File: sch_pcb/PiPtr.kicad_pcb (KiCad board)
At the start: 4 copper layers, 101.6 x 141.7 mm, 384 parts, among them J101 GLOBAL_LINK_LEFT, J102 GLOBAL_LINK_RIGHT, J107 RASPBERRY_PI, J111 FP_PIXEL, J112 AM2302, J204 DE9F, J305 AUX_IO_1, J306 SPARE, J307 SPARE, J308 AUX_IO_2, J311 I2C1_5V, J312 RTC, J315 OLED_SSD1306, J404 DE9F, J501 MicroUSB, P301 Chassis, Q101 BSS138, Q102 BSS138, Q103 BSS138, Q104 BSS138, Q105 BSS138, Q201 BSS138, Q202 BSS138, Q203 BSS138, Q401 BSS138, Q402 BSS138, Q403 BSS138, Q501 BSR315PH6327XTSA1, U101 MCP23008, U102 IP4234CZ6, U103 MCP4351, U104 74HCT138, U105 74LV1T125, U106 MCP6004T, U107 MCP4351, U108 74LVC4066, U109 74LVC1G3157, U110 74LV1T125, U111 74LV1T125, U112 74LV1T125, U113 74LV1T125, U201 MCP6004T, U202 74LVC1G3157, U203 74LVC1G3157, U204 74LVC4066, U205 MCP6004T, U206 74LVC1G3157, U207 MCP6S26, U208 MCP23008, U301 MCP23017, U304 MCP3008, U305 MCP1703A-2502/MB, U306 TPS54302, U307 IP4234CZ6, U308 IP4234CZ6, U401 MCP6004T, U402 74LVC1G3157, U403 74LVC1G3157, U404 74LVC4066, U405 MCP6004T, U406 74LVC1G3157, U407 MCP6S26, U408 MCP23008, U501 CM108B, U502 CM108B, U503 TUSB2036, U504 MCP1703A-3302/MB, U505 CM108B, Y501 6MHz

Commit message: BOM scrub
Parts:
- C501, C503, C505, C507, C513, C514, C515, C516, C517, C518, C519, C520, C533, C534, C535, C537, C538, C539: value 4u7 -> 4.7u
- C502, C504, C506, C508, C521, C522, C536, C543: value 100n -> 0.1u
- C509, C510, C511, C512, C527, C528, C540, C541, C542: footprint lib:smd0603 -> lib:smd0805
- R120: value 2200 -> 2k2
- R122: value 3300 -> 3k3
- R124: value 330R -> 100
- R214, R414: value 13k7 -> 13k3
- R325: value 511k -> SPARE
- R326: value 105k -> SPARE
- R327: value 150k -> 100k
- R503, R504, R505, R506, R507, R508, R519, R520: value 22R -> 22
- R515, R516, R523: value 33R -> 33
- moved C538 1.16 mm to (113.3, 109.0)
- moved C542 0.94 mm to (112.9, 110.4)
- moved C514 0.84 mm to (141.2, 119.5)
- moved C513 0.72 mm to (122.8, 119.7)
- moved C512 0.69 mm to (141.2, 121.1)
- moved C511 0.60 mm to (122.8, 121.2)
- moved C540 0.56 mm to (112.9, 112.1)
- moved C528 0.31 mm to (141.2, 122.9)
- moved C527 0.28 mm to (122.8, 122.9)
- moved C541 0.24 mm to (112.9, 113.9)
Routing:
- net Net-(C514-Pad1): track 3.35 -> 6.25 mm
- net Net-(C538-Pad1): track 3.11 -> 5.80 mm
- net /soundcard/TO_SND3: track 17.2 -> 16.1 mm
- net Net-(C513-Pad1): track 3.19 -> 4.14 mm
- net /soundcard/FROM_SND3: track 18.6 -> 17.8 mm
- net /soundcard/TO_SND2: track 46.6 -> 45.8 mm
- net /soundcard/FROM_SND2: track 56.8 -> 56.1 mm

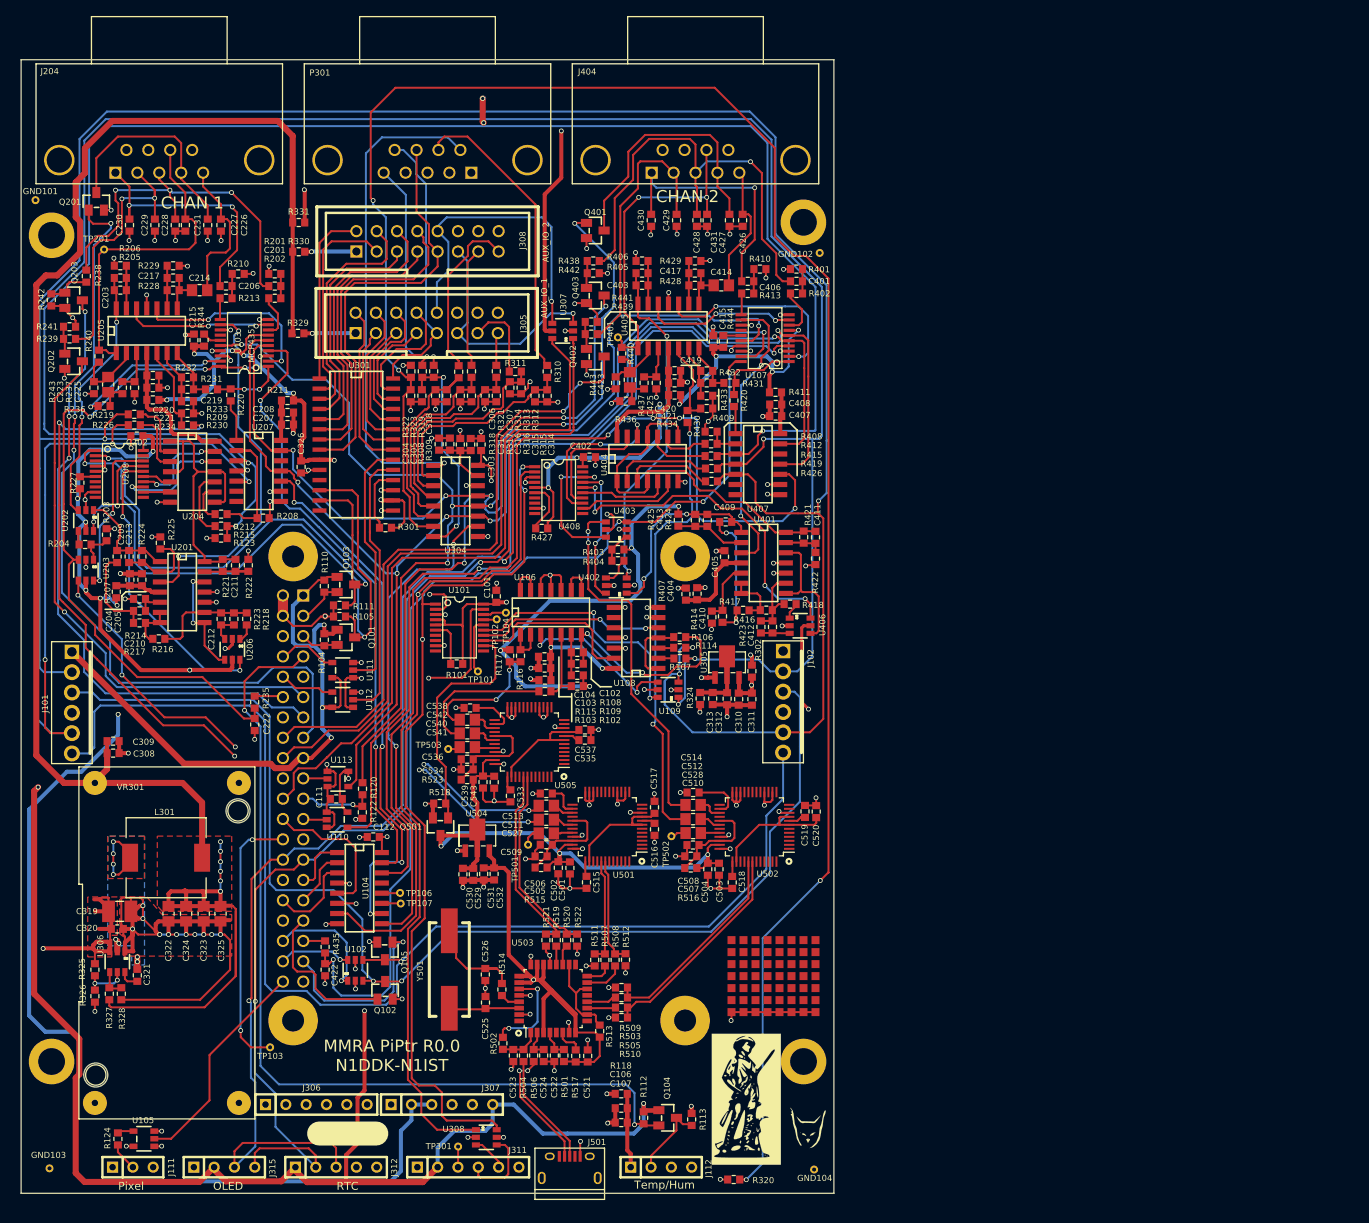
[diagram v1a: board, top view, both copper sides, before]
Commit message: Move link connector close to edge to allow using jumpers to connect boards
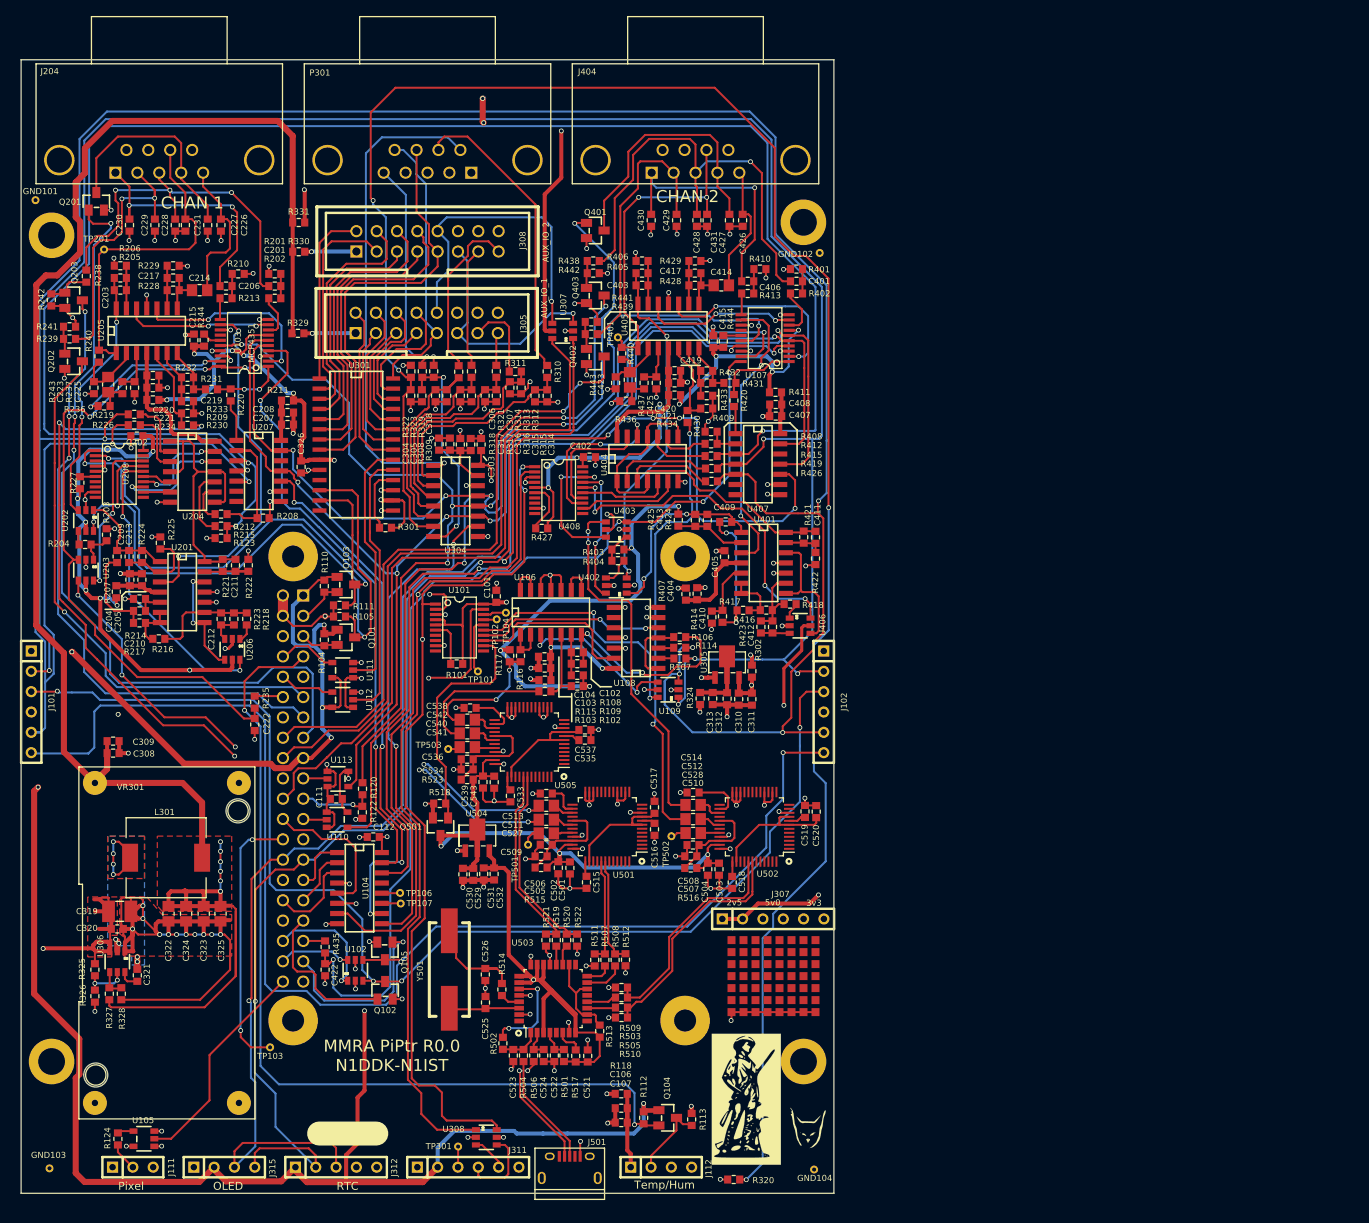
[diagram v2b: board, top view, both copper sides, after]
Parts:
- removed J306: SPARE, lib:SIL-6
- J101, J102: footprint lib:Molex_22-27-2061_100mil_6pin_verical -> lib:SIL-6
- moved J307 47.5 mm to (151.2, 135.3)
- moved J101 5.08 mm to (58.4, 108.2)
- moved J102 5.08 mm to (157.5, 108.2)
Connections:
- J307 pad 1: (no net) -> +2V5
- J307 pad 3: +2V5 -> +5V
- J307 pad 5: +5V -> +3V3
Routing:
- net +2V5: track 232.8 -> 151.7 mm, vias 38 -> 39
- net +3V3: track 528.5 -> 561.9 mm, vias 10 -> 11
- net /LINK2C: track 156.1 -> 164.8 mm, vias 1 -> 2
- net LINK2_AUD: track 370.8 -> 365.3 mm
- net /LINK1C: track 151.2 -> 155.8 mm, vias 2 -> 4
- net +5V: track 534.7 -> 532.5 mm
- net /soundcard/U2N: track 27.2 -> 29.2 mm
- net /soundcard/U2P: track 26.1 -> 28.0 mm
- net LINK1_AUD: track 302.2 -> 303.9 mm, vias 5 -> 7
- net /Spares, GPIO, and ADC/ADC_LIGHT: track 250.5 -> 251.8 mm
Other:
- board text added: "2v5"
- board text added: "3v3"
- board text added: "5v0"

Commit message: Change 33pf to 100pf.  Change 2k and 2200 to 2k2.  Change I2C addresses for MCP23008.  Nudge link connectors
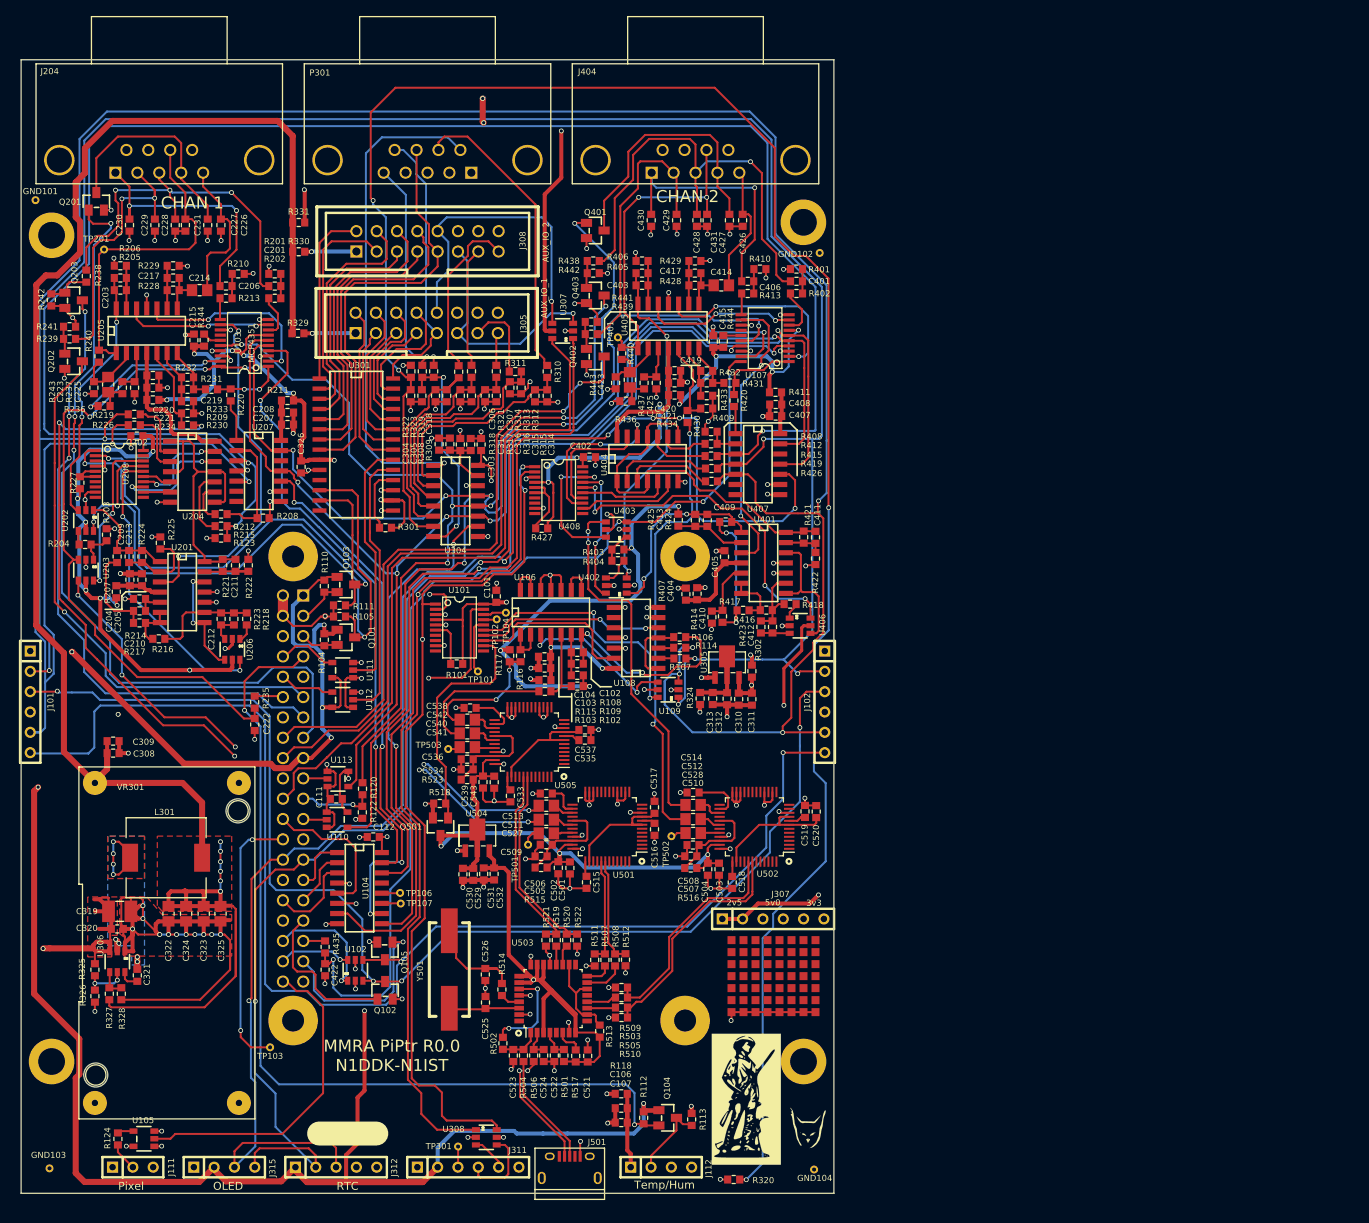
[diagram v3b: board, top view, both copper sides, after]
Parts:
- C102, C203, C211, C213, C217, C219, C403, C411, C413, C417, C419: value 33p -> 100p
- R104, R105, R107, R110, R111, R114, R212, R215, R219, R226, R412, R415, R419, R426: value 2k -> 2k2
- R308: value 2200 -> 2k2
- moved J102 0.13 mm to (157.6, 108.2)
- moved J101 0.13 mm to (58.3, 108.2)
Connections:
- J112 pad 3: (no net) -> Net-(J112-Pad3)
- J305 pad 16: (no net) -> Net-(J305-Pad16)
- J308 pad 16: (no net) -> Net-(J308-Pad16)
- J312 pad 4: Net-(J312-Pad4) -> (no net)
- J501 pad 1: (no net) -> Net-(J501-Pad1)
- J501 pad 4: (no net) -> Net-(J501-Pad4)
- MTG301 pad 1: (no net) -> Net-(MTG301-Pad1)
- MTG302 pad 1: (no net) -> Net-(MTG302-Pad1)
- MTG303 pad 1: (no net) -> Net-(MTG303-Pad1)
- MTG304 pad 1: (no net) -> Net-(MTG304-Pad1)
- U101 pad 10: Net-(U101-Pad10) -> (no net)
- U101 pad 11: Net-(U101-Pad11) -> (no net)
- U101 pad 5: +5V -> GND
- U101 pad 7: Net-(U101-Pad7) -> (no net)
- U101 pad 8: Net-(U101-Pad8) -> (no net)
- U104 pad 13: (no net) -> Net-(U104-Pad13)
- U108 pad 10: Net-(U108-Pad10) -> (no net)
- U108 pad 9: Net-(U108-Pad9) -> (no net)
- U207 pad 12: (no net) -> Net-(U207-Pad12)
- U207 pad 6: (no net) -> Net-(U207-Pad6)
- U207 pad 7: (no net) -> Net-(U207-Pad7)
- U208 pad 10: Net-(U208-Pad10) -> (no net)
- U208 pad 11: Net-(U208-Pad11) -> (no net)
- U208 pad 19: Net-(U208-Pad19) -> (no net)
- U208 pad 5: GND -> Net-(R227-Pad1)
- U208 pad 7: Net-(U208-Pad7) -> (no net)
- U208 pad 8: Net-(U208-Pad8) -> (no net)
- U407 pad 12: (no net) -> Net-(U407-Pad12)
- U407 pad 6: (no net) -> Net-(U407-Pad6)
- U407 pad 7: (no net) -> Net-(U407-Pad7)
- U408 pad 10: (no net) -> Net-(U408-Pad10)
- U408 pad 11: (no net) -> Net-(U408-Pad11)
- U408 pad 19: (no net) -> Net-(U408-Pad19)
- U408 pad 4: GND -> +5V
- U408 pad 5: +5V -> Net-(R427-Pad1)
- U408 pad 7: (no net) -> Net-(U408-Pad7)
- U408 pad 8: (no net) -> Net-(U408-Pad8)
- U501 pad 1: (no net) -> Net-(U501-Pad1)
- U501 pad 11: (no net) -> Net-(U501-Pad11)
- U501 pad 12: (no net) -> Net-(U501-Pad12)
- U501 pad 13: (no net) -> Net-(U501-Pad13)
- U501 pad 15: (no net) -> Net-(U501-Pad15)
- U501 pad 17: (no net) -> Net-(U501-Pad17)
- U501 pad 18: (no net) -> Net-(U501-Pad18)
- U501 pad 19: (no net) -> Net-(U501-Pad19)
- U501 pad 2: (no net) -> Net-(U501-Pad2)
- U501 pad 20: (no net) -> Net-(U501-Pad20)
- U501 pad 21: (no net) -> Net-(U501-Pad21)
- U501 pad 25: (no net) -> Net-(U501-Pad25)
- U501 pad 28: (no net) -> Net-(U501-Pad28)
- U501 pad 3: (no net) -> Net-(U501-Pad3)
- U501 pad 31: (no net) -> Net-(U501-Pad31)
- U501 pad 39: (no net) -> Net-(U501-Pad39)
- U501 pad 4: (no net) -> Net-(U501-Pad4)
- U501 pad 40: (no net) -> Net-(U501-Pad40)
- U501 pad 43: (no net) -> Net-(U501-Pad43)
- U501 pad 44: (no net) -> Net-(U501-Pad44)
- U501 pad 45: (no net) -> Net-(U501-Pad45)
- U501 pad 46: (no net) -> Net-(U501-Pad46)
- U501 pad 47: (no net) -> Net-(U501-Pad47)
- U501 pad 48: (no net) -> Net-(U501-Pad48)
- U501 pad 5: (no net) -> Net-(U501-Pad5)
- U501 pad 6: (no net) -> Net-(U501-Pad6)
- U502 pad 1: (no net) -> Net-(U502-Pad1)
- U502 pad 11: (no net) -> Net-(U502-Pad11)
- U502 pad 12: (no net) -> Net-(U502-Pad12)
- U502 pad 13: (no net) -> Net-(U502-Pad13)
- U502 pad 15: (no net) -> Net-(U502-Pad15)
- U502 pad 17: (no net) -> Net-(U502-Pad17)
- U502 pad 18: (no net) -> Net-(U502-Pad18)
- U502 pad 19: (no net) -> Net-(U502-Pad19)
- U502 pad 2: (no net) -> Net-(U502-Pad2)
- U502 pad 20: (no net) -> Net-(U502-Pad20)
- U502 pad 21: (no net) -> Net-(U502-Pad21)
- U502 pad 25: (no net) -> Net-(U502-Pad25)
- U502 pad 28: (no net) -> Net-(U502-Pad28)
- U502 pad 3: (no net) -> Net-(U502-Pad3)
- U502 pad 31: (no net) -> Net-(U502-Pad31)
- U502 pad 39: (no net) -> Net-(U502-Pad39)
- U502 pad 4: (no net) -> Net-(U502-Pad4)
- U502 pad 40: (no net) -> Net-(U502-Pad40)
- U502 pad 43: (no net) -> Net-(U502-Pad43)
- U502 pad 44: (no net) -> Net-(U502-Pad44)
- U502 pad 45: (no net) -> Net-(U502-Pad45)
- U502 pad 46: (no net) -> Net-(U502-Pad46)
- U502 pad 47: (no net) -> Net-(U502-Pad47)
- U502 pad 48: (no net) -> Net-(U502-Pad48)
- U502 pad 5: (no net) -> Net-(U502-Pad5)
- U502 pad 6: (no net) -> Net-(U502-Pad6)
- U503 pad 13: (no net) -> Net-(U503-Pad13)
- U503 pad 17: (no net) -> Net-(U503-Pad17)
- U503 pad 32: (no net) -> Net-(U503-Pad32)
- U503 pad 5: (no net) -> Net-(U503-Pad5)
- U503 pad 9: (no net) -> Net-(U503-Pad9)
- U505 pad 1: Net-(U505-Pad1) -> (no net)
- U505 pad 11: Net-(U505-Pad11) -> (no net)
- U505 pad 12: Net-(U505-Pad12) -> (no net)
- U505 pad 13: Net-(U505-Pad13) -> (no net)
- U505 pad 15: Net-(U505-Pad15) -> (no net)
- U505 pad 17: Net-(U505-Pad17) -> (no net)
- U505 pad 18: Net-(U505-Pad18) -> (no net)
- U505 pad 19: Net-(U505-Pad19) -> (no net)
- U505 pad 2: Net-(U505-Pad2) -> (no net)
- U505 pad 20: Net-(U505-Pad20) -> (no net)
- U505 pad 21: Net-(U505-Pad21) -> (no net)
- U505 pad 25: Net-(U505-Pad25) -> (no net)
- U505 pad 28: Net-(U505-Pad28) -> (no net)
- U505 pad 3: Net-(U505-Pad3) -> (no net)
- U505 pad 31: Net-(U505-Pad31) -> (no net)
- U505 pad 39: Net-(U505-Pad39) -> (no net)
- U505 pad 4: Net-(U505-Pad4) -> (no net)
- U505 pad 40: Net-(U505-Pad40) -> (no net)
- U505 pad 43: Net-(U505-Pad43) -> (no net)
- U505 pad 44: Net-(U505-Pad44) -> (no net)
- U505 pad 45: Net-(U505-Pad45) -> (no net)
- U505 pad 46: Net-(U505-Pad46) -> (no net)
- U505 pad 47: Net-(U505-Pad47) -> (no net)
- U505 pad 48: Net-(U505-Pad48) -> (no net)
- U505 pad 5: Net-(U505-Pad5) -> (no net)
- U505 pad 6: Net-(U505-Pad6) -> (no net)
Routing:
- net /PIXEL_33: track 27.8 -> 40.9 mm
- net Net-(R227-Pad1): track 1.93 -> 4.14 mm
- net GND: track 365.9 -> 367.9 mm, vias 154 -> 155
- net Net-(R427-Pad1): track 6.62 -> 8.46 mm
- net +5V: track 532.5 -> 531.0 mm
